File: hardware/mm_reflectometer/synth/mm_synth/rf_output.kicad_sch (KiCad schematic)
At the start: 4 parts

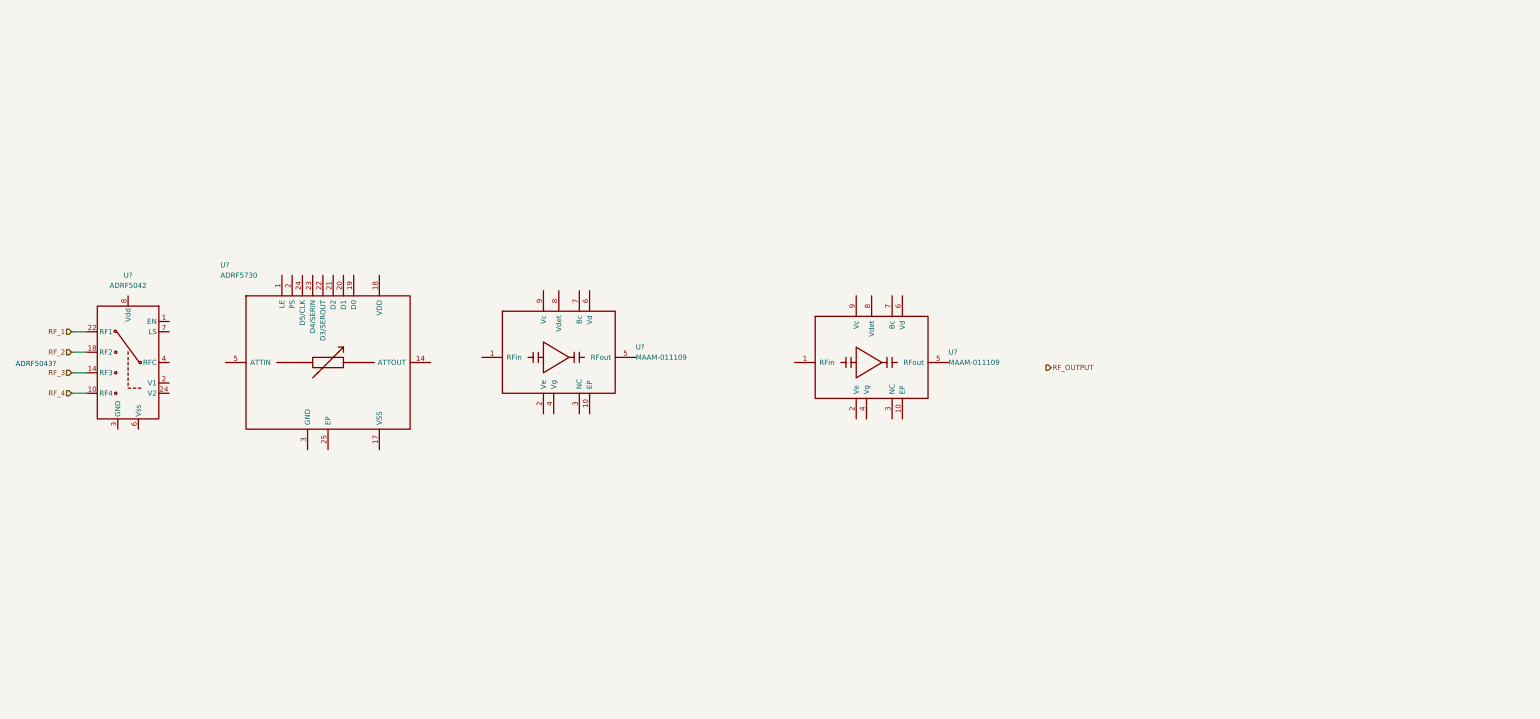
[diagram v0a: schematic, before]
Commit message: adding bias circuitry to mm synth
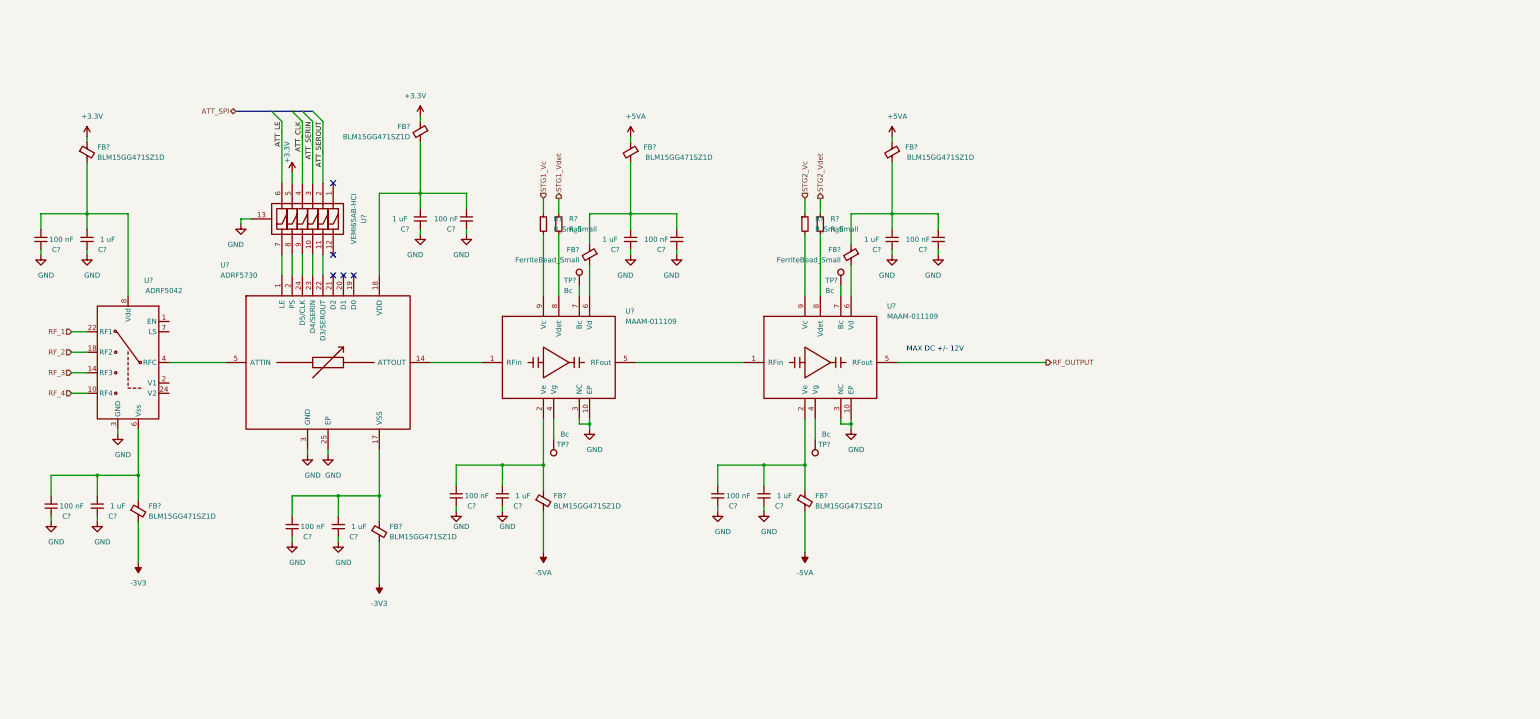
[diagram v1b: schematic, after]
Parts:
- added C? (x8): 100 nF, symbol Device:C_Small
- added C? (x8): 1 uF, symbol Device:C_Small
- added FB? (x8): BLM15GG471SZ1D, symbol Device:FerriteBead_Small
- added FB? (x2): FerriteBead_Small, symbol Device:FerriteBead_Small
- added R? (x4): R_Small, symbol Device:R_Small
- added TP? (x4): Bc, symbol Connector:TestPoint
- added U?: VEMI65AB-HCI, symbol vna_mm:VEMI65AB-HCI
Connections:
- net GND: now also U?.10 (EP), U?.10 (EP), U?.11 (GND), U?.12 (GND), U?.13 (GND), U?.15 (GND), U?.16 (GND), U?.17 (GND), U?.19 (GND), U?.20 (GND), U?.21 (GND), U?.23 (GND), U?.25 (EP), U?.25 (GND), U?.3 (GND), U?.3 (NC), U?.3 (NC), U?.5 (GND), U?.9 (GND), C?.1, C?.1, C?.1, C?.1, C?.1, C?.1, C?.1, C?.1, C?.1, C?.1, C?.1, C?.1, C?.1, C?.1, C?.1, C?.1, U?.13
- net RF_OUTPUT: now also U?.5 (RFout)
- net at U?.1 (RFin): now also U?.14 (ATTOUT)
- net at U?.2 (Ve): now also C?.2, C?.2, FB?.1 (x2)
- net at U?.4 (Vg): now also TP?.1 (x2)
- net at U?.5 (RFout): now also U?.1 (RFin)
- net at U?.6 (Vd): now also FB?.2 (x2)
- net at U?.7 (Bc): now also TP?.1 (x2)
- net at U?.8 (Vdet): now also R?.2 (x2)
- net at U?.9 (Vc): now also R?.2 (x2)
- net at U?.1 (LE): now also U?.7
- net at U?.17 (VSS): now also C?.2, C?.2, FB?.1
- net at U?.18 (VDD): now also C?.2, C?.2, FB?.2
- net at U?.2 (PS): now also U?.8
- net at U?.22 (D3/SEROUT): now also U?.11
- net at U?.23 (D4/SERIN): now also U?.10
- net at U?.24 (D5/CLK): now also U?.9
- net at U?.5 (ATTIN): now also U?.4 (RFC)
- net at U?.6 (Vss): now also C?.2, C?.2, FB?.1
- net at U?.8 (Vdd): now also C?.2, C?.2, FB?.2
- new net: C?.2, C?.2, FB?.1, FB?.2 (x2)
- new net +3V3: FB?.1, FB?.1, U?.5
- new net +5VA: FB?.1, FB?.1
- new net -3V3: FB?.2, FB?.2
- new net -5VA: FB?.2, FB?.2
- new net ATT_CLK: U?.4
- new net ATT_LE: U?.6
- new net ATT_SERIN: U?.3
- new net ATT_SEROUT: U?.2
- new net STG1_Vc: R?.1
- new net STG1_Vdet: R?.1
- new net STG2_Vc: R?.1
- new net STG2_Vdet: R?.1
- no-connect marks 0 -> 5
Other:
- note added: "MAX DC +/- 12V"
- note removed: "ADRF5043?"
- moved on the sheet: U?

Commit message: schematic work on mm synth -- starting voltage regulation
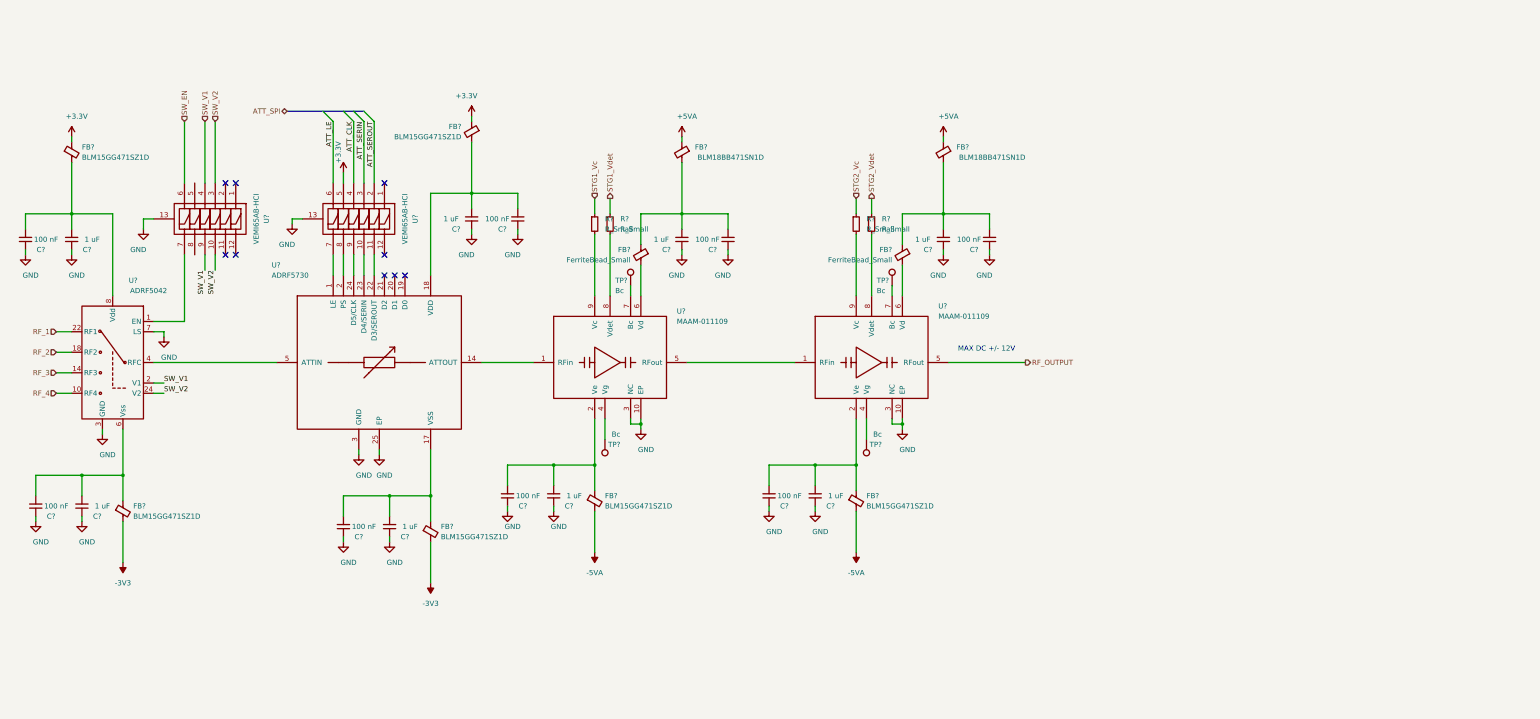
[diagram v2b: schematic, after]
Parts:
- added U?: VEMI65AB-HCI, symbol vna_mm:VEMI65AB-HCI
- FB? (x2): value BLM15GG471SZ1D -> BLM18BB471SN1D
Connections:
- net GND: now also U?.7 (LS), U?.13
- net at U?.1 (EN): now also U?.7
- net SW_V1: now reaches U?.2 (V1)
- net SW_V1: now also U?.4, U?.9
- net SW_V2: now reaches U?.24 (V2)
- net SW_V2: now also U?.10, U?.3
- new net SW_EN: U?.6
- no-connect marks 5 -> 9
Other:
- moved on the sheet: C?, FB?, R?, TP?, U?

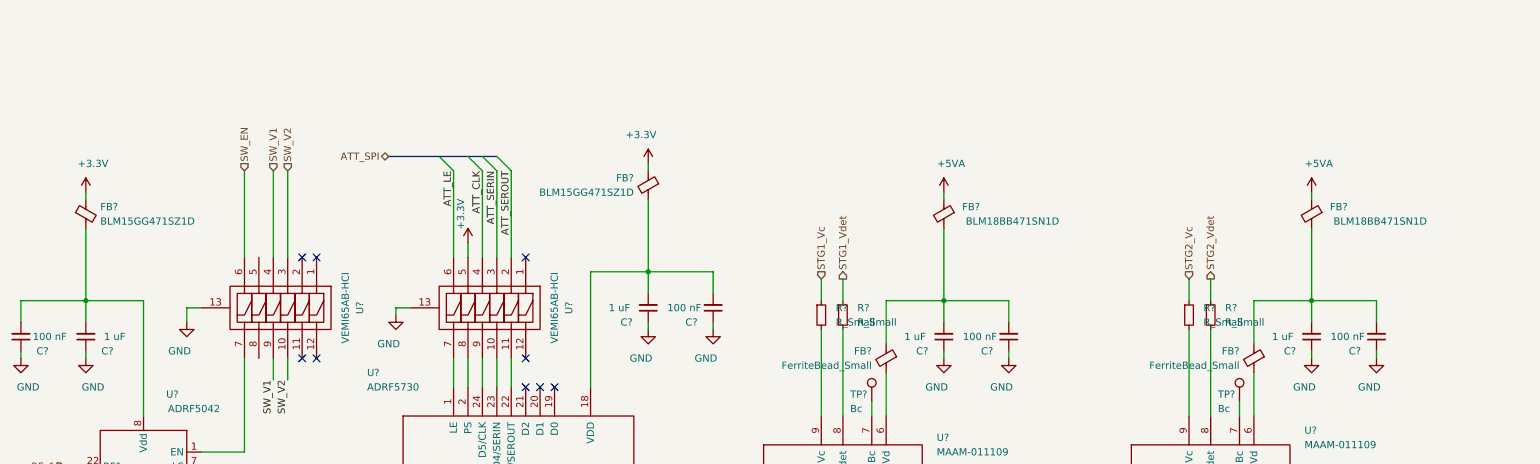
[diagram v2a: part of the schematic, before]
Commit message: adding digital connections to synth schematic
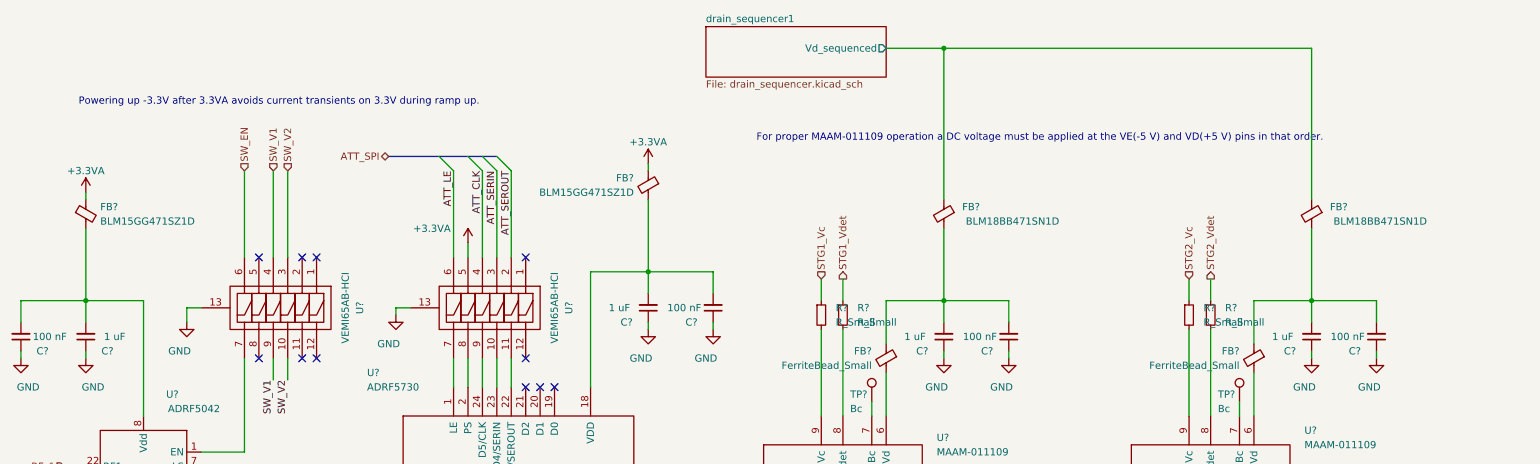
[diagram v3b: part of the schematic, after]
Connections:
- net +3V3 renamed +3.3VA
- net +5VA renamed drain_sequencer1/Vd_sequenced
- no-connect marks 9 -> 11
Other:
- added sheet drain_sequencer1 (drain_sequencer.kicad_sch)
- note added: "For proper MAAM-011109 operation a DC voltage must be applied at the VE(-5 V) and VD(+5 V) pins in that order."
- note added: "Powering up -3.3V after 3.3VA avoids current transients on 3.3V during ramp up."
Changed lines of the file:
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@@
   (junction (at 160.02 133.35) (diameter 0.9144) (color 0 0 0 0))
   (junction (at 171.45 123.19) (diameter 0.9144) (color 0 0 0 0))
+  (junction (at 181.61 26.67) (diameter 0.9144) (color 0 0 0 0))
   (junction (at 181.61 71.12) (diameter 0.9144) (color 0 0 0 0))
   (junction (at 214.63 133.35) (diameter 0.9144) (color 0 0 0 0))
@@
   (junction (at 236.22 123.19) (diameter 0.9144) (color 0 0 0 0))
   (junction (at 246.38 71.12) (diameter 0.9144) (color 0 0 0 0))
+  (no_connect (at 60.96 63.5))
+  (no_connect (at 60.96 81.28))
   (no_connect (at 68.58 63.5))
   (no_connect (at 68.58 81.28))
@@
     (stroke (width 0) (type solid) (color 0 0 0 0))
   )
+  (wire (pts (xy 171.45 26.67) (xy 181.61 26.67))
+    (stroke (width 0) (type solid) (color 0 0 0 0))
+  )
   (wire (pts (xy 171.45 71.12) (xy 171.45 78.74))
     (stroke (width 0) (type solid) (color 0 0 0 0))
@@
     (stroke (width 0) (type solid) (color 0 0 0 0))
   )
-  (wire (pts (xy 181.61 52.07) (xy 181.61 53.34))
+  (wire (pts (xy 181.61 26.67) (xy 181.61 53.34))
+    (stroke (width 0) (type solid) (color 0 0 0 0))
+  )
+  (wire (pts (xy 181.61 26.67) (xy 246.38 26.67))
     (stroke (width 0) (type solid) (color 0 0 0 0))
   )
@@
     (stroke (width 0) (type solid) (color 0 0 0 0))
   )
-  (wire (pts (xy 246.38 52.07) (xy 246.38 53.34))
+  (wire (pts (xy 246.38 26.67) (xy 246.38 53.34))
     (stroke (width 0) (type solid) (color 0 0 0 0))
   )
@@
   (bus (pts (xy 83.82 45.72) (xy 102.87 45.72))
     (stroke (width 0) (type solid) (color 0 0 0 0))
+  )
+  (text "Powering up -3.3V after 3.3VA avoids current transients on 3.3V during ramp up."
+    (at 29.21 36.83 0)
+    (effects (font (size 1.27 1.27)) (justify left bottom))
+  )
+  (text "For proper MAAM-011109 operation a DC voltage must be applied at the VE(-5 V) and VD(+5 V) pins in that order."
+    (at 148.59 43.18 0)
+    (effects (font (size 1.27 1.27)) (justify left bottom))
   )
   (text "MAX DC +/- 12V" (at 264.16 105.41 180)
@@
     (effects (font (size 1.27 1.27)) (justify left))
   )
-  (symbol (lib_id "power:+3.3V") (at 30.48 52.07 0) (unit 1)
-    (in_bom yes) (on_board yes)
+  (symbol (lib_id "power:+3.3VA") (at 30.48 52.07 0) (unit 1)
+    (in_bom yes) (on_board yes) (fields_autoplaced)
     (property "Reference" "#PWR?" (id 0) (at 30.48 55.88 0)
       (effects (font (size 1.27 1.27)) hide)
     )
-    (property "Value" "+3.3V" (id 1) (at 31.75 46.99 0))
+    (property "Value" "+3.3VA" (id 1) (at 30.48 48.26 0))
     (property "Footprint" "" (id 2) (at 30.48 52.07 0)
       (effects (font (size 1.27 1.27)) hide)
@@
     (pin "1")
   )
-  (symbol (lib_id "power:+3.3V") (at 97.79 60.96 0) (mirror y) (unit 1)
+  (symbol (lib_id "power:+3.3VA") (at 97.79 60.96 0) (unit 1)
     (in_bom yes) (on_board yes)
     (property "Reference" "#PWR?" (id 0) (at 97.79 64.77 0)
       (effects (font (size 1.27 1.27)) hide)
     )
-    (property "Value" "+3.3V" (id 1) (at 96.52 55.88 90))
+    (property "Value" "+3.3VA" (id 1) (at 91.44 58.42 0))
     (property "Footprint" "" (id 2) (at 97.79 60.96 0)
       (effects (font (size 1.27 1.27)) hide)
@@
     (pin "1")
   )
-  (symbol (lib_id "power:+3.3V") (at 129.54 46.99 0) (mirror y) (unit 1)
-    (in_bom yes) (on_board yes)
+  (symbol (lib_id "power:+3.3VA") (at 129.54 46.99 0) (unit 1)
+    (in_bom yes) (on_board yes) (fields_autoplaced)
     (property "Reference" "#PWR?" (id 0) (at 129.54 50.8 0)
       (effects (font (size 1.27 1.27)) hide)
     )
-    (property "Value" "+3.3V" (id 1) (at 128.27 41.91 0))
+    (property "Value" "+3.3VA" (id 1) (at 129.54 43.18 0))
     (property "Footprint" "" (id 2) (at 129.54 46.99 0)
       (effects (font (size 1.27 1.27)) hide)
@@
     (pin "1")
   )
-  (symbol (lib_id "power:+5VA") (at 181.61 52.07 0) (unit 1)
-    (in_bom yes) (on_board yes)
-    (property "Reference" "#PWR?" (id 0) (at 181.61 55.88 0)
-      (effects (font (size 1.27 1.27)) hide)
-    )
-    (property "Value" "+5VA" (id 1) (at 182.88 46.99 0))
-    (property "Footprint" "" (id 2) (at 181.61 52.07 0)
-      (effects (font (size 1.27 1.27)) hide)
-    )
-    (property "Datasheet" "" (id 3) (at 181.61 52.07 0)
-      (effects (font (size 1.27 1.27)) hide)
-    )
-    (pin "1")
-  )
   (symbol (lib_id "power:-5VA") (at 224.79 154.94 180) (unit 1)
     (in_bom yes) (on_board yes)
@@
     )
     (property "Datasheet" "" (id 3) (at 224.79 154.94 0)
-      (effects (font (size 1.27 1.27)) hide)
-    )
-    (pin "1")
-  )
-  (symbol (lib_id "power:+5VA") (at 246.38 52.07 0) (unit 1)
-    (in_bom yes) (on_board yes)
-    (property "Reference" "#PWR?" (id 0) (at 246.38 55.88 0)
-      (effects (font (size 1.27 1.27)) hide)
-    )
-    (property "Value" "+5VA" (id 1) (at 247.65 46.99 0))
-    (property "Footprint" "" (id 2) (at 246.38 52.07 0)
-      (effects (font (size 1.27 1.27)) hide)
-    )
-    (property "Datasheet" "" (id 3) (at 246.38 52.07 0)
       (effects (font (size 1.27 1.27)) hide)
     )
@@
     (pin "9")
   )
+  (sheet (at 139.7 22.86) (size 31.75 8.89)
+    (stroke (width 0.001) (type solid) (color 0 0 0 0))
+    (fill (color 0 0 0 0.0000))
+    (property "Sheet name" "drain_sequencer1" (id 0) (at 139.7 22.2241 0)
+      (effects (font (size 1.27 1.27)) (justify left bottom))
+    )
+    (property "Sheet file" "drain_sequencer.kicad_sch" (id 1) (at 139.7 32.2589 0)
+      (effects (font (size 1.27 1.27)) (justify left top))
+    )
+    (pin "Vd_sequenced" output (at 171.45 26.67 0)
+      (effects (font (size 1.27 1.27)) (justify right))
+    )
+  )
 )
